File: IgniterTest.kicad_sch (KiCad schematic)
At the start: 16 parts

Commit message: okokok
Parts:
- BV1, CV1, CV2, Needle_Valve1, PT1, PT2, PT3, PT4: value (none) -> ~
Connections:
- net at Fuel_Main_Servo1.: now also CV2.; no longer Fuel_Tank1.
- net at Needle_Valve1.: now also Fuel_Press1., N2_Reg1.
- net at N2_Bottle1.: now also N2_Reg1.
- net at N2O_Bottle1.: now also Ox_Main_Servo1.
- net at Ox_Main_Servo1.: now also CV1.; no longer N2O_Bottle1.
- new net: CV2., PT3., Torch_Ignitor1.
- new net: CV1., PT1., Torch_Ignitor1.
- new net: Fuel_Main_Servo1., Fuel_Tank1.
- now unconnected: PT1., PT3.
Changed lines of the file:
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@@
 			)
 		)
-		(property "Value" ""
+		(property "Value" "~"
 			(at 139.7 158.75 0)
 			(effects
@@
 			)
 		)
-		(property "Value" ""
+		(property "Value" "~"
 			(at 151.13 71.12 0)
 			(effects
@@
 	)
 	(symbol
-		(lib_name "PID_symbols:Pressure_Transducer")
 		(lib_id "PID_symbols:Pressure_Transducer")
 		(at 139.7 149.86 0)
@@
 			)
 		)
-		(property "Value" ""
+		(property "Value" "~"
 			(at 139.7 151.13 0)
 			(effects
@@
 	)
 	(symbol
-		(lib_name "PID_symbols:Pressure_Transducer")
 		(lib_id "PID_symbols:Pressure_Transducer")
 		(at 111.76 149.86 0)
@@
 			)
 		)
-		(property "Value" ""
+		(property "Value" "~"
 			(at 111.76 151.13 0)
 			(effects
@@
 			)
 		)
-		(property "Value" ""
+		(property "Value" "~"
 			(at 116.84 134.62 0)
 			(effects
@@
 	)
 	(symbol
-		(lib_name "PID_symbols:Check_Valve")
 		(lib_id "PID_symbols:Check_Valve")
 		(at 134.62 134.62 270)
@@
 			)
 		)
-		(property "Value" ""
+		(property "Value" "~"
 			(at 134.62 134.62 0)
 			(effects
@@
 	)
 	(symbol
-		(lib_name "PID_symbols:Pressure_Transducer")
 		(lib_id "PID_symbols:Pressure_Transducer")
 		(at 127 90.17 0)
@@
 			)
 		)
-		(property "Value" ""
+		(property "Value" "~"
 			(at 127 91.44 0)
 			(effects
@@
 			)
 		)
-		(property "Value" ""
+		(property "Value" "~"
 			(at 151.13 90.17 0)
 			(effects

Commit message: Updated igniter PID
+PT +nitrous pressure
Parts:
- added PT2: ~, symbol PID:Pressure_Transducer
- added Reg1: ~, symbol PID:Pressure_Regulator
- renumbered PT2 to PT1, PT1 to PT3, PT3 to PT4, PT4 to PT5
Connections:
- net at Fuel_Main_Servo1.: now also CV2.; no longer Fuel_Tank1.
- net at Needle_Valve1.: now also Fuel_Press1., N2_Reg1.
- net at N2_Bottle1.: now also N2_Reg1.
- net at N2O_Bottle1.: now also Reg1.
- net at Ox_Main_Servo1.: now also CV1.; no longer N2O_Bottle1.
- new net: CV2., PT4., Torch_Ignitor1.
- new net: CV1., PT3., Torch_Ignitor1.
- new net: Fuel_Main_Servo1., Fuel_Tank1.
- new net: Ox_Main_Servo1., PT2., Reg1.
- now unconnected: PT3., PT4.
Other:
- moved on the sheet: N2O_Bottle1
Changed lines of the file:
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@@
 		(color 0 0 0 0)
 	)
+	(junction
+		(at 116.84 107.95)
+		(diameter 0)
+		(color 0 0 0 0)
+	)
 	(wire
 		(pts
@@
 	(wire
 		(pts
+			(xy 116.84 107.95) (xy 116.84 113.03)
+		)
+		(stroke
+			(width 0)
+			(type default)
+		)
+	)
+	(wire
+		(pts
 			(xy 134.62 71.12) (xy 148.59 71.12)
 		)
@@
 	(wire
 		(pts
+			(xy 116.84 105.41) (xy 116.84 107.95)
+		)
+		(stroke
+			(width 0)
+			(type default)
+		)
+	)
+	(wire
+		(pts
 			(xy 133.35 157.48) (xy 137.16 157.48)
 		)
@@
 	(wire
 		(pts
-			(xy 116.84 107.95) (xy 116.84 113.03)
+			(xy 106.68 107.95) (xy 116.84 107.95)
 		)
 		(stroke
@@
 		(pts
 			(xy 116.84 125.73) (xy 116.84 132.08)
+		)
+		(stroke
+			(width 0)
+			(type default)
+		)
+	)
+	(wire
+		(pts
+			(xy 116.84 86.36) (xy 116.84 92.71)
 		)
 		(stroke
@@
 	)
 	(symbol
+		(lib_name "PID_symbols:Pressure_Transducer")
 		(lib_id "PID_symbols:Pressure_Transducer")
 		(at 139.7 157.48 0)
@@
 		(on_board yes)
 		(dnp no)
-		(property "Reference" "PT4"
+		(property "Reference" "PT5"
 			(at 139.7 161.29 0)
 			(effects
@@
 			(project "P_IDs"
 				(path "/045f1f05-3134-4b6d-91b6-463031104f1e/6a55bbd5-ed21-4b79-a194-d378f68dea1b"
-					(reference "PT4")
+					(reference "PT5")
 					(unit 1)
 				)
@@
 	)
 	(symbol
+		(lib_name "PnID_symbols:Tank")
 		(lib_id "PnID_symbols:Tank")
 		(at 133.35 52.07 0)
@@
 	)
 	(symbol
+		(lib_name "PnID_symbols:Tank")
 		(lib_id "PnID_symbols:Tank")
 		(at 133.35 105.41 0)
@@
 	)
 	(symbol
+		(lib_name "PID_symbols:Pressure_Transducer")
 		(lib_id "PID_symbols:Pressure_Transducer")
 		(at 139.7 149.86 0)
@@
 		(on_board yes)
 		(dnp no)
-		(property "Reference" "PT3"
+		(property "Reference" "PT4"
 			(at 139.7 153.67 0)
 			(effects
@@
 			(project "P_IDs"
 				(path "/045f1f05-3134-4b6d-91b6-463031104f1e/6a55bbd5-ed21-4b79-a194-d378f68dea1b"
-					(reference "PT3")
+					(reference "PT4")
 					(unit 1)
 				)
@@
 	)
 	(symbol
+		(lib_name "PID_symbols:Pressure_Transducer")
 		(lib_id "PID_symbols:Pressure_Transducer")
 		(at 111.76 149.86 0)
@@
 		(on_board yes)
 		(dnp no)
-		(property "Reference" "PT1"
+		(property "Reference" "PT3"
 			(at 111.76 153.67 0)
 			(effects
@@
 			(project "P_IDs"
 				(path "/045f1f05-3134-4b6d-91b6-463031104f1e/6a55bbd5-ed21-4b79-a194-d378f68dea1b"
-					(reference "PT1")
+					(reference "PT3")
 					(unit 1)
 				)
@@
 	)
 	(symbol
+		(lib_name "PnID_symbols:Tank")
 		(lib_id "PnID_symbols:Tank")
-		(at 115.57 105.41 0)
+		(at 115.57 83.82 0)
 		(unit 1)
 		(exclude_from_sim no)
@@
 		(dnp no)
 		(property "Reference" "N2O_Bottle1"
-			(at 101.346 100.33 0)
+			(at 101.346 78.74 0)
 			(effects
 				(font
@@
 		)
 		(property "Value" "~"
-			(at 121.92 102.235 0)
+			(at 121.92 80.645 0)
 			(effects
 				(font
@@
 		)
 		(property "Footprint" ""
-			(at 115.57 105.41 0)
-			(effects
-				(font
-					(size 1.27 1.27)
-				)
-				(hide yes)
-			)
-		)
-		(property "Datasheet" ""
-			(at 115.57 105.41 0)
+			(at 115.57 83.82 0)
+			(effects
+				(font
+					(size 1.27 1.27)
+				)
+				(hide yes)
+			)
+		)
+		(property "Datasheet" ""
+			(at 115.57 83.82 0)
 			(effects
 				(font
@@
 		)
 		(property "Description" ""
-			(at 115.57 105.41 0)
+			(at 115.57 83.82 0)
 			(effects
 				(font
@@
 	)
 	(symbol
+		(lib_id "PID:Pressure_Regulator")
+		(at 116.84 95.25 270)
+		(unit 1)
+		(exclude_from_sim no)
+		(in_bom yes)
+		(on_board yes)
+		(dnp no)
+		(fields_autoplaced yes)
+		(property "Reference" "Reg1"
+			(at 121.92 98.4874 90)
+			(effects
+				(font
+					(size 1.27 1.27)
+				)
+				(justify left)
+			)
+		)
+		(property "Value" "~"
+			(at 121.92 100.3925 90)
+			(effects
+				(font
+					(size 1.27 1.27)
+				)
+				(justify left)
+			)
+		)
+		(property "Footprint" ""
+			(at 116.84 95.25 0)
+			(effects
+				(font
+					(size 1.27 1.27)
+				)
+				(hide yes)
+			)
+		)
+		(property "Datasheet" ""
+			(at 116.84 95.25 0)
+			(effects
+				(font
+					(size 1.27 1.27)
+				)
+				(hide yes)
+			)
+		)
+		(property "Description" "Pressure Regulator"
+			(at 110.49 99.06 0)
+			(effects
+				(font
+					(size 1.27 1.27)
+				)
+				(hide yes)
+			)
+		)
+		(pin ""
+		)
+		(pin ""
+		)
+		(instances
+			(project ""
+				(path "/045f1f05-3134-4b6d-91b6-463031104f1e/6a55bbd5-ed21-4b79-a194-d378f68dea1b"
+					(reference "Reg1")
+					(unit 1)
+				)
+			)
+		)
+	)
+	(symbol
+		(lib_name "PID_symbols:Check_Valve")
 		(lib_id "PID_symbols:Check_Valve")
 		(at 116.84 134.62 270)
@@
 	)
 	(symbol
+		(lib_name "PID_symbols:Check_Valve")
 		(lib_id "PID_symbols:Check_Valve")
 		(at 134.62 134.62 270)
@@
 	)
 	(symbol
+		(lib_name "PID_symbols:Pressure_Transducer")
 		(lib_id "PID_symbols:Pressure_Transducer")
 		(at 127 90.17 0)
@@
 		(on_board yes)
 		(dnp no)
-		(property "Reference" "PT2"
+		(property "Reference" "PT1"
 			(at 127 93.98 0)
 			(effects
@@
 			(project "P_IDs"
 				(path "/045f1f05-3134-4b6d-91b6-463031104f1e/6a55bbd5-ed21-4b79-a194-d378f68dea1b"
-					(reference "PT2")
+					(reference "PT1")
 					(unit 1)
 				)
@@
 					(unit 1)
 				)
+			)
+		)
+	)
+	(symbol
+		(lib_id "PID:Pressure_Transducer")
+		(at 104.14 107.95 0)
+		(unit 1)
+		(exclude_from_sim no)
+		(in_bom yes)
+		(on_board yes)
+		(dnp no)
+		(fields_autoplaced yes)
+		(property "Reference" "PT2"
+			(at 104.14 102.87 0)
+			(effects
+				(font
+					(size 1.27 1.27)
+				)
+			)
+		)
+		(property "Value" "~"
+			(at 104.14 109.22 0)
+			(effects
+				(font
+					(size 1.27 1.27)
+				)
+				(hide yes)
+			)
+		)
+		(property "Footprint" ""
+			(at 104.14 107.95 0)
+			(effects
+				(font
+					(size 1.27 1.27)
+				)
+				(hide yes)
+			)
+		)
+		(property "Datasheet" ""
+			(at 104.14 107.95 0)
+			(effects
+				(font
+					(size 1.27 1.27)
+				)
+				(hide yes)
+			)
+		)
+		(property "Description" ""
+			(at 104.14 107.95 0)
+			(effects
+				(font
+					(size 1.27 1.27)
+				)
+				(hide yes)
+			)
+		)
+		(pin ""
+		)
+		(pin ""
+		)
+		(pin ""
+		)
+		(instances
+			(project ""
+				(path "/045f1f05-3134-4b6d-91b6-463031104f1e/6a55bbd5-ed21-4b79-a194-d378f68dea1b"
+					(reference "PT2")
+					(unit 1)
+				)

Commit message: replaced servo with solenoid
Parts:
- removed BV1: ~, symbol PID_symbols:Ball_Valve
- added nO_Sol1: ~, symbol PID:Normally Open Solenoid
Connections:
- net at Fuel_Main_Servo1.: now also CV2.; no longer Fuel_Tank1.
- net at Needle_Valve1.: now also Fuel_Press1., N2_Reg1.
- net at N2_Bottle1.: now also N2_Reg1.
- net at Fuel_Press1., Fuel_Tank1., PT1.: now also nO_Sol1.
- net at N2O_Bottle1.: now also Reg1.
- net at Reg1.: now also Ox_Main_Servo1., PT2.; no longer N2O_Bottle1.
- new net: CV2., PT4., Torch_Ignitor1.
- new net: CV1., PT3., Torch_Ignitor1.
- new net: Fuel_Main_Servo1., Fuel_Tank1.
- now unconnected: PT2., PT3., PT4.
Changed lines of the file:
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@@
+	)
+	(symbol
+		(lib_id "PID:Normally Open Solenoid")
+		(at 151.13 90.17 0)
+		(unit 1)
+		(exclude_from_sim no)
+		(in_bom yes)
+		(on_board yes)
+		(dnp no)
+		(fields_autoplaced yes)
+		(property "Reference" "nO_Sol1"
+			(at 154.94 81.28 0)
+			(effects
+				(font
+					(size 1.27 1.27)
+				)
+			)
+		)
+		(property "Value" "~"
+			(at 154.94 83.82 0)
+			(effects
+				(font
+					(size 1.27 1.27)
+				)
+			)
+		)
+		(property "Footprint" ""
+			(at 151.13 90.17 0)
+			(effects
+				(font
+					(size 1.27 1.27)
+				)
+				(hide yes)
+			)
+		)
+		(property "Datasheet" ""
+			(at 151.13 90.17 0)
+			(effects
+				(font
+					(size 1.27 1.27)
+				)
+				(hide yes)
+			)
+		)
+		(property "Description" ""
+			(at 151.13 90.17 0)
+			(effects
+				(font
+					(size 1.27 1.27)
+				)
+				(hide yes)
+			)
+		)
+		(pin ""
+		)
+		(pin ""
+		)
+		(instances
+			(project ""
+				(path "/045f1f05-3134-4b6d-91b6-463031104f1e/6a55bbd5-ed21-4b79-a194-d378f68dea1b"
+					(reference "nO_Sol1")
+					(unit 1)
+				)
+			)
+		)
 	)
 	(symbol
@@
 					(unit 1)
 				)
-			)
-		)
-	)
-	(symbol
-		(lib_id "PID_symbols:Ball_Valve")
-		(at 151.13 90.17 0)
-		(unit 1)
-		(exclude_from_sim no)
-		(in_bom yes)
-		(on_board yes)
-		(dnp no)
-		(property "Reference" "BV1"
-			(at 154.94 94.488 0)
-			(effects
-				(font
-					(size 1.27 1.27)
-				)
-			)
-		)
-		(property "Value" "~"
-			(at 151.13 90.17 0)
-			(effects
-				(font
-					(size 1.27 1.27)
-				)
-			)
-		)
-		(property "Footprint" ""
-			(at 151.13 90.17 0)
-			(effects
-				(font
-					(size 1.27 1.27)
-				)
-				(hide yes)
-			)
-		)
-		(property "Datasheet" ""
-			(at 151.13 90.17 0)
-			(effects
-				(font
-					(size 1.27 1.27)
-				)
-				(hide yes)
-			)
-		)
-		(property "Description" ""
-			(at 151.13 90.17 0)
-			(effects
-				(font
-					(size 1.27 1.27)
-				)
-				(hide yes)
-			)
-		)
-		(pin ""
-		)
-		(pin ""
-		)
-		(instances
-			(project "P_IDs"
-				(path "/045f1f05-3134-4b6d-91b6-463031104f1e/6a55bbd5-ed21-4b79-a194-d378f68dea1b"
-					(reference "BV1")
-					(unit 1)
-				)
-			)
-			(project "IgniterTest"
-				(path "/1fe58bd7-d6db-4cdb-9816-3cf1e5c4b0ec"
-					(reference "Fuel_Vent_Servo")
-					(unit 1)
-				)

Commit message: rebase
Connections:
- net at Fuel_Main_Servo1.: now also CV2.; no longer Fuel_Tank1.
- net at Needle_Valve1.: now also Fuel_Press1., N2_Reg1.
- net at N2_Bottle1.: now also N2_Reg1.
- net at N2O_Bottle1.: now also Reg1.
- net at Reg1.: now also Ox_Main_Servo1., PT2.; no longer N2O_Bottle1.
- new net: CV2., PT4., Torch_Ignitor1.
- new net: CV1., PT3., Torch_Ignitor1.
- new net: Fuel_Main_Servo1., Fuel_Tank1.
- now unconnected: PT2., PT3., PT4.
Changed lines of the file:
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@@
 	)
 	(symbol
-		(lib_name "PID_symbols:Pressure_Transducer")
 		(lib_id "PID_symbols:Pressure_Transducer")
 		(at 139.7 157.48 0)
@@
 	)
 	(symbol
-		(lib_name "PnID_symbols:Tank")
 		(lib_id "PnID_symbols:Tank")
 		(at 133.35 52.07 0)
@@
 	)
 	(symbol
-		(lib_name "PnID_symbols:Tank")
 		(lib_id "PnID_symbols:Tank")
 		(at 133.35 105.41 0)
@@
 	)
 	(symbol
-		(lib_name "PID_symbols:Pressure_Transducer")
 		(lib_id "PID_symbols:Pressure_Transducer")
 		(at 139.7 149.86 0)
@@
 	)
 	(symbol
-		(lib_name "PID_symbols:Pressure_Transducer")
 		(lib_id "PID_symbols:Pressure_Transducer")
 		(at 111.76 149.86 0)
@@
 	)
 	(symbol
-		(lib_name "PnID_symbols:Tank")
 		(lib_id "PnID_symbols:Tank")
 		(at 115.57 83.82 0)
@@
 	)
 	(symbol
-		(lib_name "PID_symbols:Check_Valve")
 		(lib_id "PID_symbols:Check_Valve")
 		(at 116.84 134.62 270)
@@
 	)
 	(symbol
-		(lib_name "PID_symbols:Check_Valve")
 		(lib_id "PID_symbols:Check_Valve")
 		(at 134.62 134.62 270)
@@
 	)
 	(symbol
-		(lib_name "PID_symbols:Pressure_Transducer")
 		(lib_id "PID_symbols:Pressure_Transducer")
 		(at 127 90.17 0)

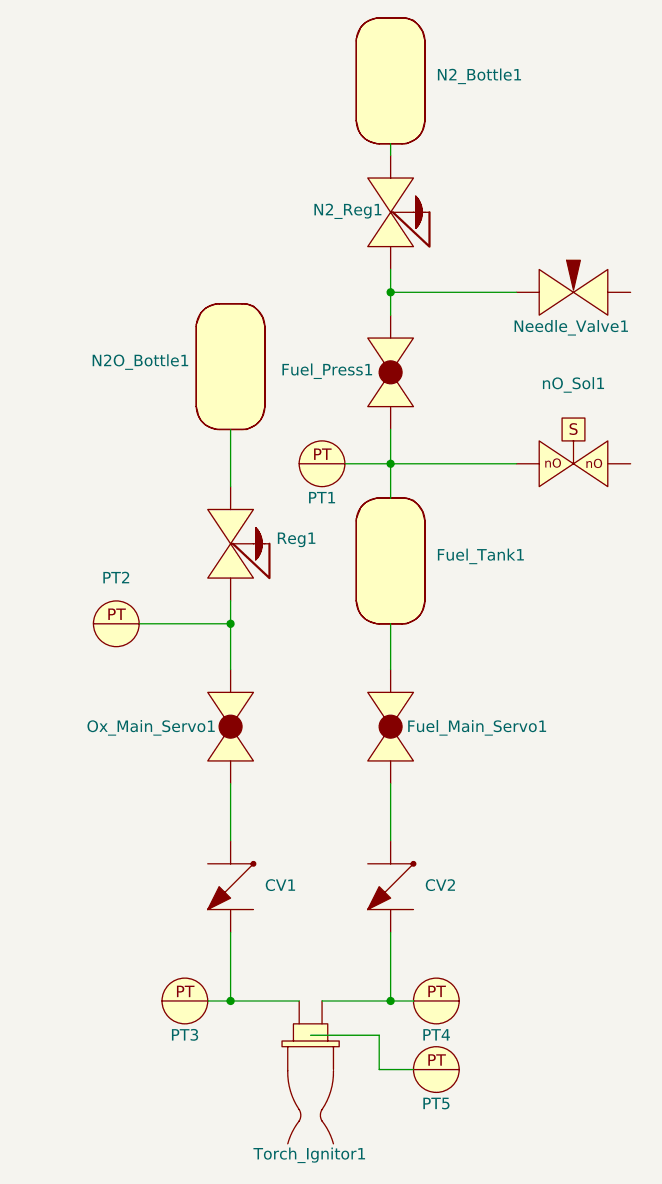
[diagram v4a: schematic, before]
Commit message: Updated PID to test set up
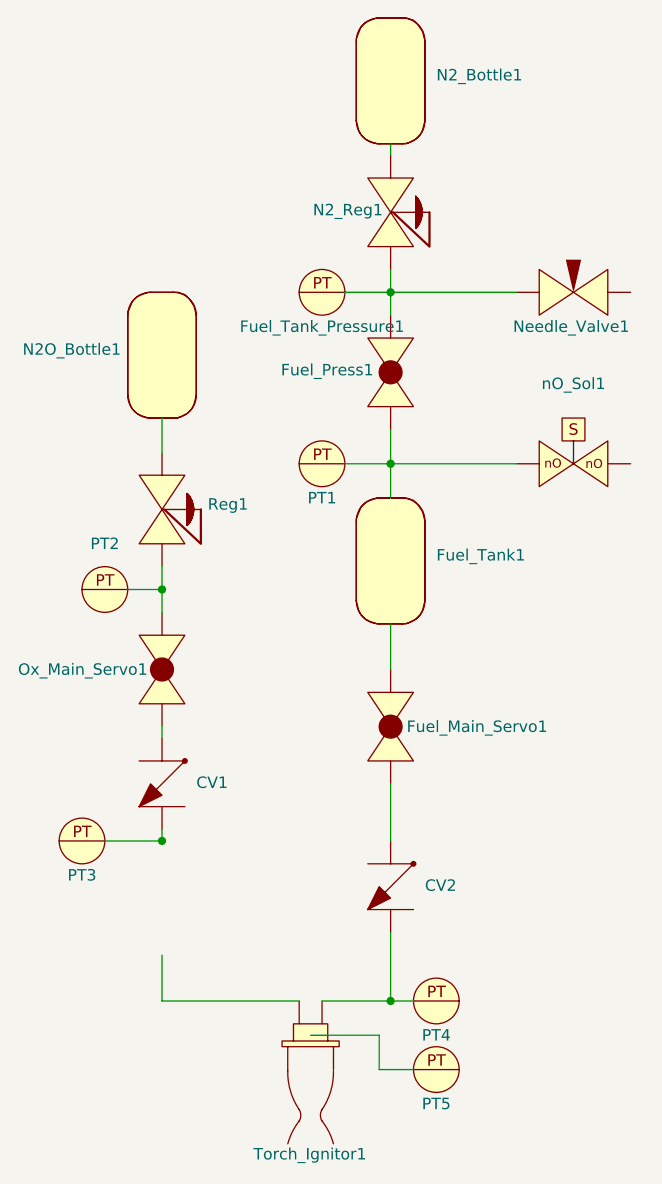
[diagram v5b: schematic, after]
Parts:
- added Fuel_Tank_Pressure1: ~, symbol PID_symbols:Pressure_Transducer
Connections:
- net at Fuel_Main_Servo1.: now also CV2.; no longer Fuel_Tank1.
- net at N2_Bottle1.: now also N2_Reg1.
- net at PT3.: now also CV1.
- net at N2O_Bottle1.: now also Reg1.
- net at Reg1.: now also Ox_Main_Servo1., PT2.; no longer N2O_Bottle1.
- new net: CV2., PT4., Torch_Ignitor1.
- new net: Fuel_Main_Servo1., Fuel_Tank1.
- new net: Fuel_Press1., Fuel_Tank_Pressure1., N2_Reg1., Needle_Valve1.
- now unconnected: Needle_Valve1., PT2., PT4.
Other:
- moved on the sheet: CV1, N2O_Bottle1, Ox_Main_Servo1, PT2, PT3, Reg1
